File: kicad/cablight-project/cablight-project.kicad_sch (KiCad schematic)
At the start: 58 parts, among them J3 Screw_Term_1x4_5mm, Q1 IRLB8721PBF, SW3 switch_SPDT_SLW_121586, T1 ISL85410, U1 TPD2EUSB30, U3 ESP32-S3-WROOM-1U

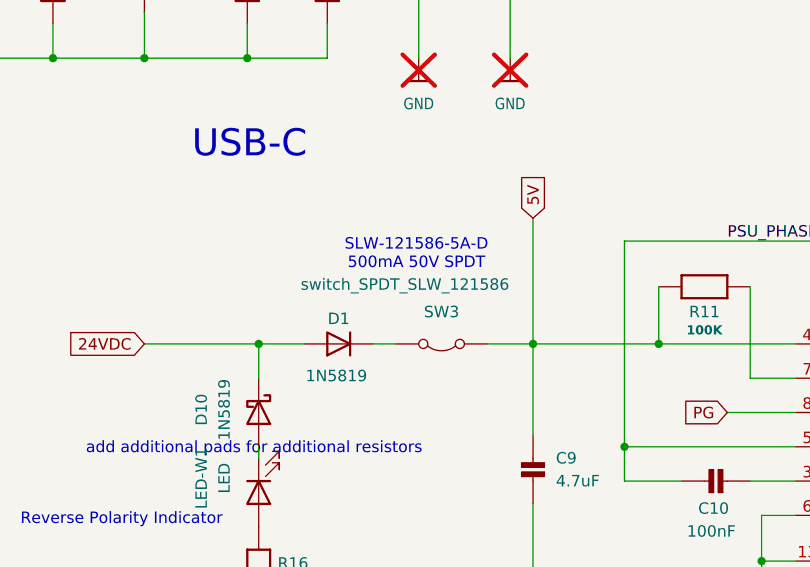
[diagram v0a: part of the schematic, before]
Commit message: create more space for usb esd
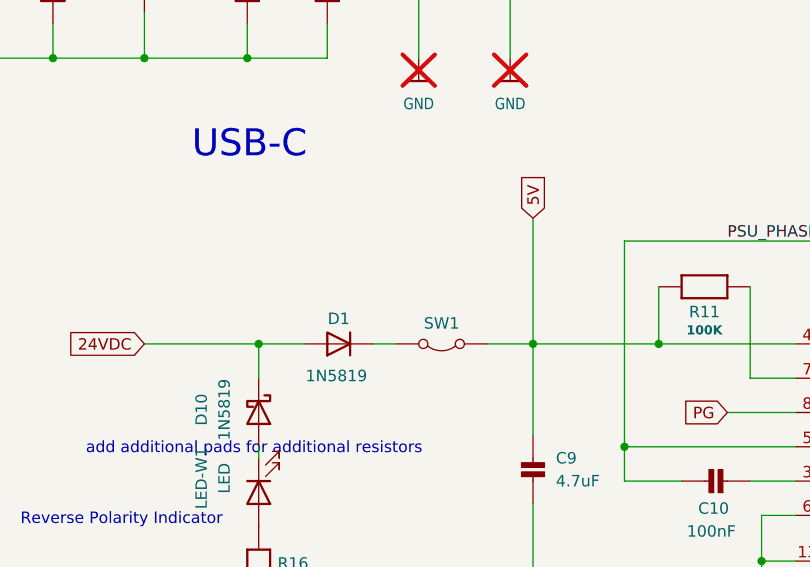
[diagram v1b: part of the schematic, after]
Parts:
- SW1: renamed from SW3; footprint Connector_PinHeader_2.54mm:PinHeader_1x02_P2.54mm_Vertical -> GRK_Lib:1x02_P2.54mm_Vertical_Shunt
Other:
- note removed: "SLW-121586-5A-D 500mA 50V SPDT"
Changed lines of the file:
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@@
 		)
 	)
-	(text "SLW-121586-5A-D\n500mA 50V SPDT"
-		(exclude_from_sim no)
-		(at 98.806 203.454 0)
-		(effects
-			(font
-				(size 1.27 1.27)
-			)
-		)
-	)
 	(text "Reverse Polarity Indicator\n"
 		(exclude_from_sim no)
@@
 		(on_board yes)
 		(dnp no)
-		(property "Reference" "SW3"
-			(at 101.6 209.804 0)
+		(property "Reference" "SW1"
+			(at 101.6 211.074 0)
 			(effects
 				(font
@@
 					(size 1.27 1.27)
 				)
+				(hide yes)
 			)
 		)
-		(property "Footprint" "Connector_PinHeader_2.54mm:PinHeader_1x02_P2.54mm_Vertical"
+		(property "Footprint" "GRK_Lib:1x02_P2.54mm_Vertical_Shunt"
 			(at 101.6 213.36 0)
 			(effects
@@
 			(project "cablight-project"
 				(path "/2aa36568-293b-470b-bbef-a9ff44d0879c"
-					(reference "SW3")
+					(reference "SW1")
 					(unit 1)
 				)

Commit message: schematic cleanup
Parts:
- removed D3, D5: ESD321, GRK_Lib:ESD321_SOT5x3_DYA_TEX, symbol Diode:1N5819
- B1: renamed from RESET1; value Tactile -> RESET - TACTILE SMD
- B2: renamed from BOOT1; value tactile -> BOOT - TACTILE SMD
- C5: value 10uF -> 22uF
- LED1: renamed from LED-W1; value LED -> LED 0603
- LED2: renamed from LED-OK1; value LED -> LED 0603
- SW1: value switch_SPDT_SLW_121586 -> SHUNT JUMPER
- renumbered D10 to D2, D2 to D3, J3 to J1, RCWL-1601 to J2, USBC-V1 to USBC1
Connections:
- net GND: now also DIP1.1
- net LEDSIG: no longer DIP1.1
- net DIP0: now reaches U3.9 (GPIO16/U0CTS/ADC2_CH5/XTAL_32K_N)
- net DIP0: now also DIP1.8
- net 3.3V renamed 3V3
- net 3V3: no longer DIP1.8
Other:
- note added: "LED LOAD SWITCHING"
- note added: "REVERSE POLARITY INDICATOR (RED)"
- note removed: "CONSULT DATASHEET FOR IMPORTANT UART PINS ETC"
- note removed: "Reverse Polarity Indicator"
- note removed: "TODO: weak pulldown to gnd? for sbu pins?"
- note removed: "can also use SMD NSR0320"
- note removed: "findo out what IO corresponts to what GPIO? I think I can pick which ones I want."
- note removed: "i may forgo esd protection as usb plugging duty cycle isn't high enough for likely wrongful insertions. USB is only for flashing & debugging."
- moved on the sheet: B1, B2, BTN1, C10, C11, C12, C14, C3, C4, C5, C6, C7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
